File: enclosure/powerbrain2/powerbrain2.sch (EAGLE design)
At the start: 45 parts, among them J3 AVR_SPI_PRG_6PTH, Q1 FDD4141TO252, Q2 200mA/50V, Q3 200mA/50V, U2 TPS61090, X2 ZX62D-B-5PA8

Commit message: powerbrain2 sent to fab
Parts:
- removed BC1: 10uF, SparkFun-Capacitors:CAP1206
- removed BC2: 2.2uF, SparkFun-Capacitors:CAP1206
- removed BL1: 6.8uH / 2A, SparkFun-Passives:INDUCTORSRU5028
- removed BR1, BR3: 1.87M, SparkFun-Resistors:RESISTOR1206
- removed BR2: 340k, SparkFun-Resistors:RESISTOR1206
- removed BR4: 200k, SparkFun-Resistors:RESISTOR1206
- removed BR5: (no value), SparkFun-Resistors:RESISTOR1206
- removed C7: 100uF / 6V, SparkFun-Passives:CAP_POL3528-KIT
- removed H4: MOUNT-HOLE2.8, holes:MOUNT-HOLE2.8
- removed U2: TPS61090, TPS61090:TPS61090
- added J5: (no value), SparkFun-Connectors:M03LOCK
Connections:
- removed net B_FB: BR3.2, BR4.1, U2.FB
- removed net B_LBI: BR1.1, BR2.2, U2.LBI
- removed net B_SW: BL1.1, U2.SW@1, U2.SW@2
- removed net LOW_BATTERY_OUTPUT: BR5.2, U2.LBO
- net BATT_GND: no longer BC1.2, BC2.1, BR2.1, BR4.2, C7.-, U2.GND, U2.PGND@1, U2.PGND@2, U2.PGND@3, U2.POWER_PAD, U2.SYNC
- net BATT_VCC: now also J5.3; no longer BC1.1, BL1.2, BR1.2, U2.EN, U2.VBAT
- net GND: now also J5.2
- net VCC: now also J5.1; no longer BC2.2, BR3.1, BR5.1, C7.+, U2.VOUT@1, U2.VOUT@2, U2.VOUT@3

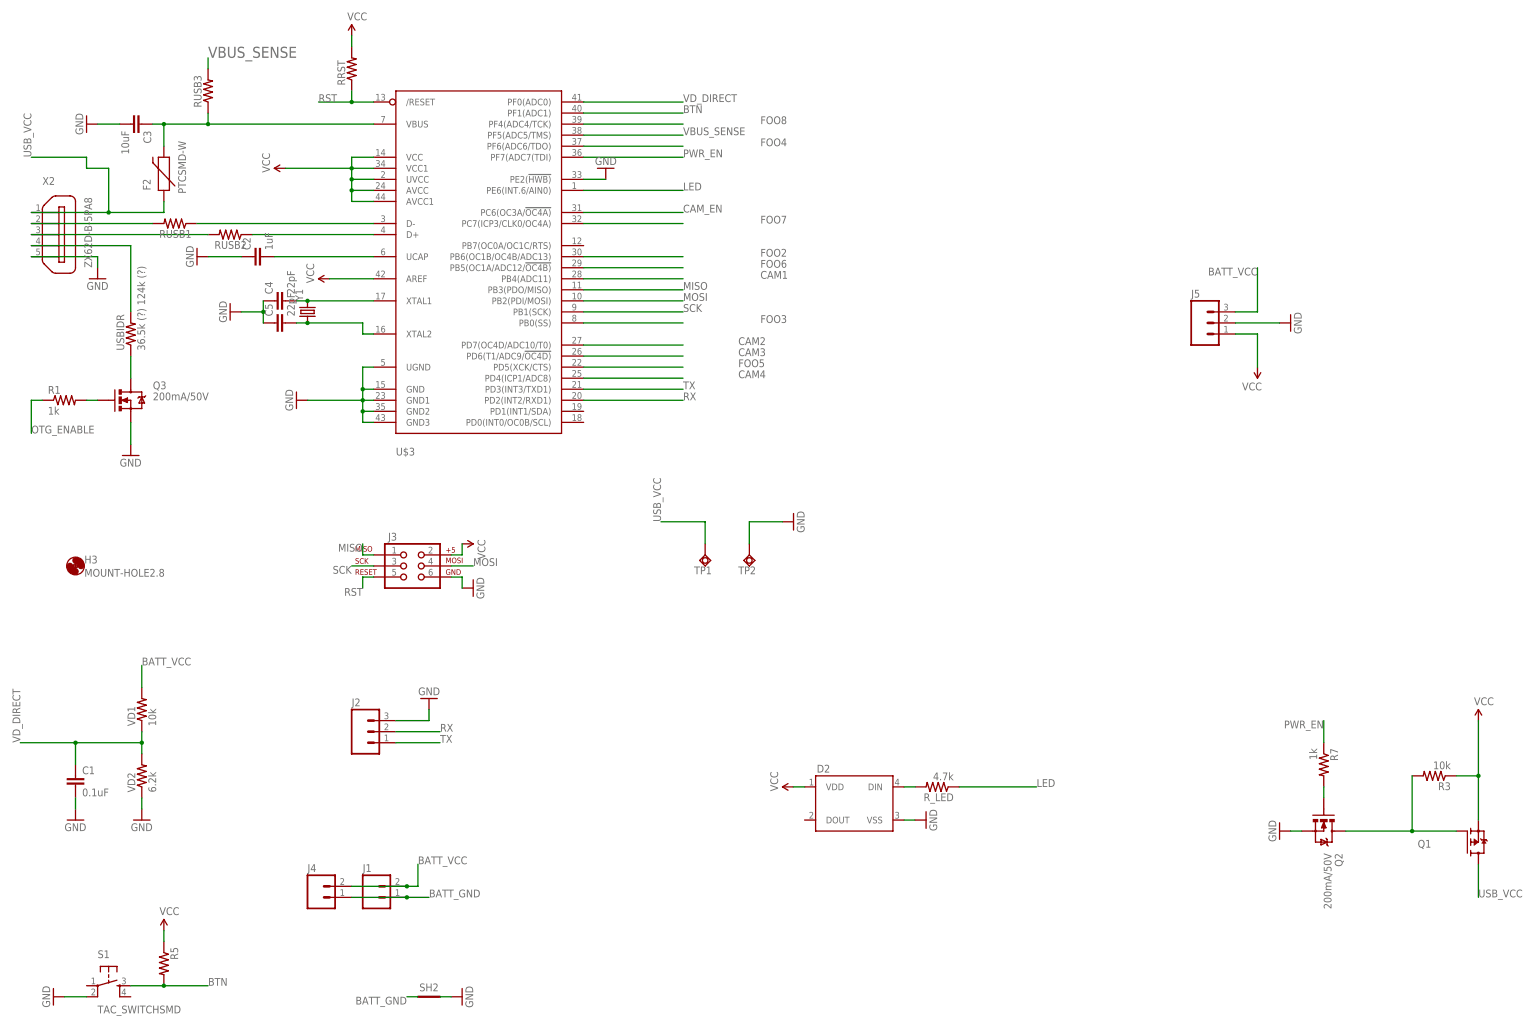
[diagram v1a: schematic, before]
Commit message: cleaned up the powerbrain2 schematics
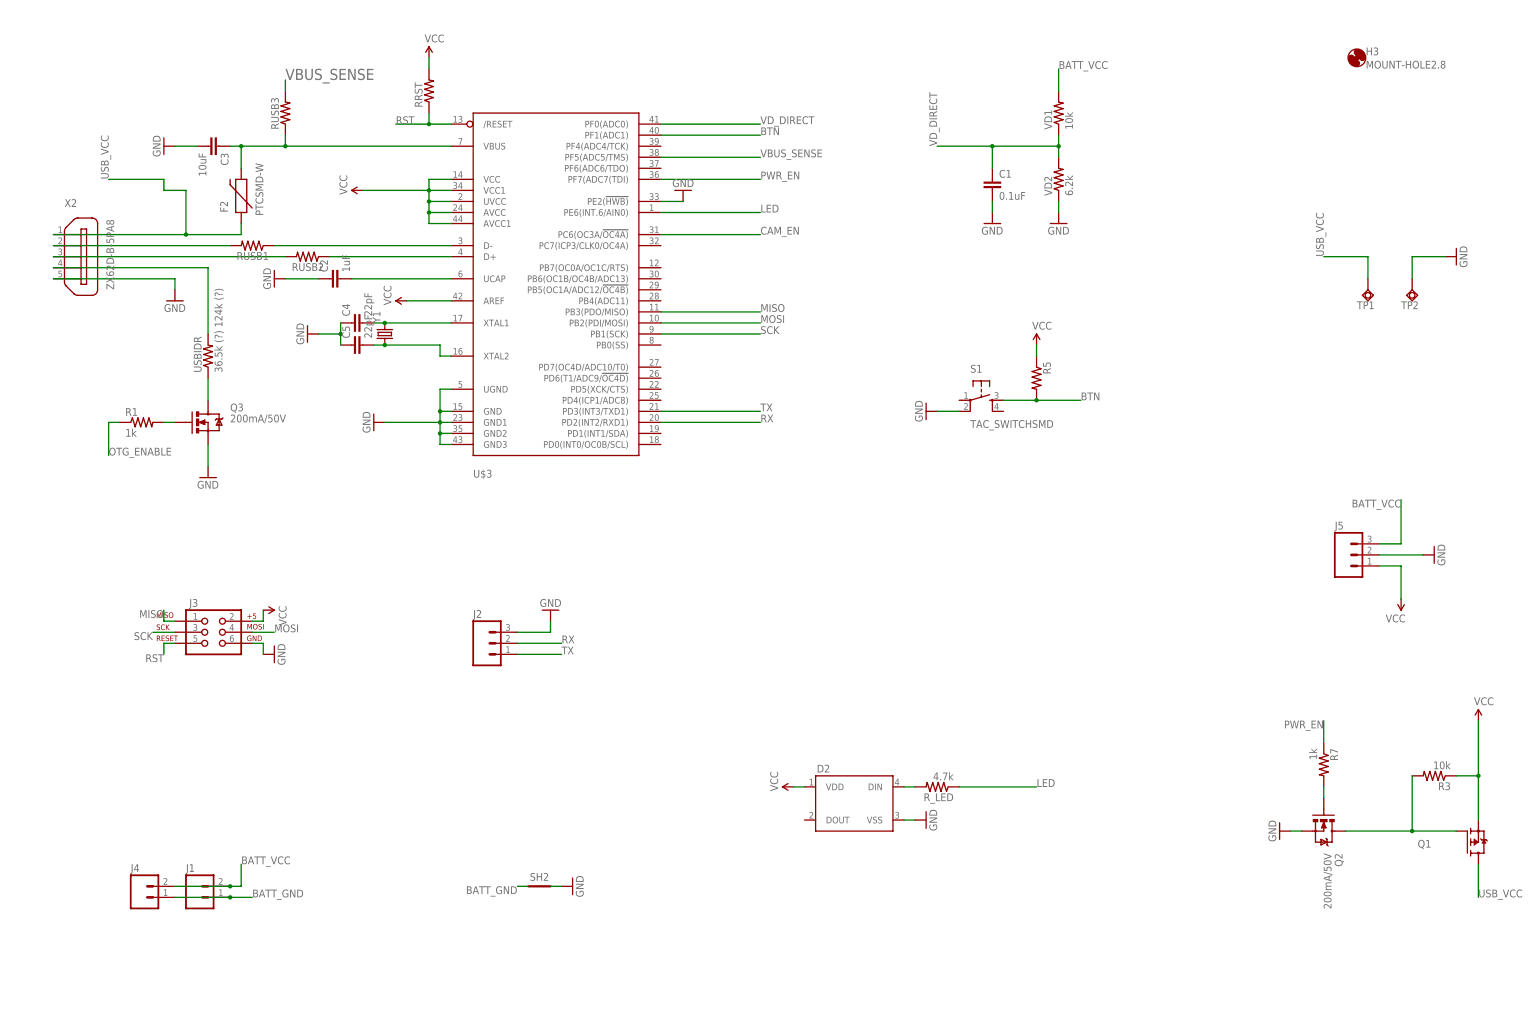
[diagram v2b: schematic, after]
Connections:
- removed net CAM1: U$3.PB4(ADC11)
- removed net CAM2: U$3.PD7(OC4D/ADC10/T0)
- removed net CAM3: U$3.PD6(T1/ADC9/!OC4D)
- removed net CAM4: U$3.PD4(ICP1/ADC8)
- removed net FOO2: U$3.PB6(OC1B/OC4B/ADC13)
- removed net FOO3: U$3.PB0(SS)
- removed net FOO4: U$3.PF6(ADC6/TDO)
- removed net FOO5: U$3.PD5(XCK/CTS)
- removed net FOO6: U$3.PB5(OC1A/ADC12/!OC4B)
- removed net FOO7: U$3.PC7(ICP3/CLK0/OC4A)
- removed net FOO8: U$3.PF4(ADC4/TCK)
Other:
- moved on the sheet: C1, C2, C3, C4, C5, F2, H3, J1, J2, J3, J4, J5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
